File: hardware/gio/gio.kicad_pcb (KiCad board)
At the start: 2 copper layers, 20 x 108 mm, 55 parts, among them J1 PJ3001F, J2 PJ3001F, J3 oled, J4 eurorack power, J5 PJ3001F, J6 PJ3001F, SW1 encoder, U1 TL072, U2 MCP3208, U3 DAC8552, U5 TL072, U6 AMS1117CD-5.0, U7 REF3040, U8 XIAO-RP2350-DIP_pins_only

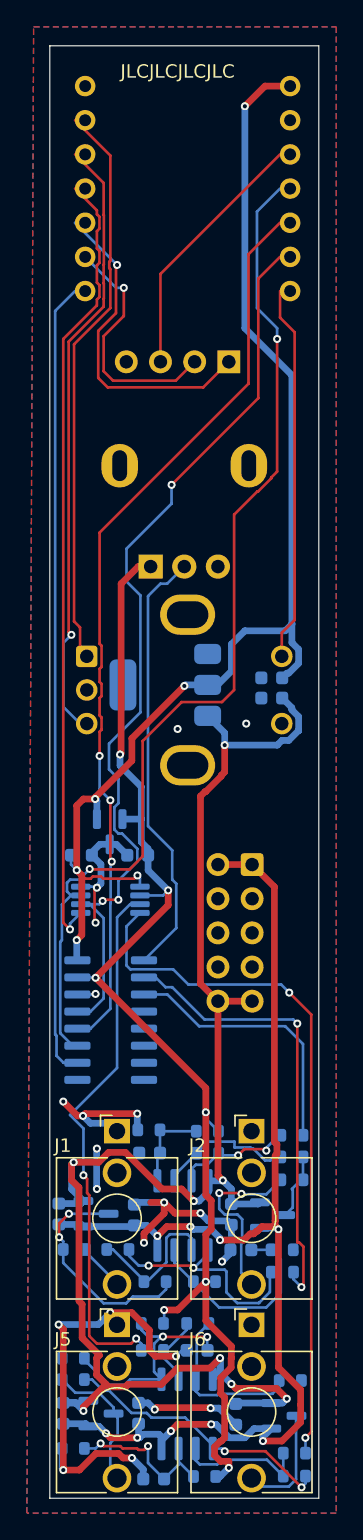
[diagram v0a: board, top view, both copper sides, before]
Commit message: PCB routing progress + zone min_clearance relaxed to 0
Continuation of the layout work from "just ratsnest" (672885e). The
project file also drops board.design_settings.rules.zones.min_clearance
from 0.5 mm to 0.0 — a deliberate design-rule relaxation, not an
autosave artifact.

Co-Authored-By: Claude Opus 4.7 (1M context) <noreply@anthropic.com>
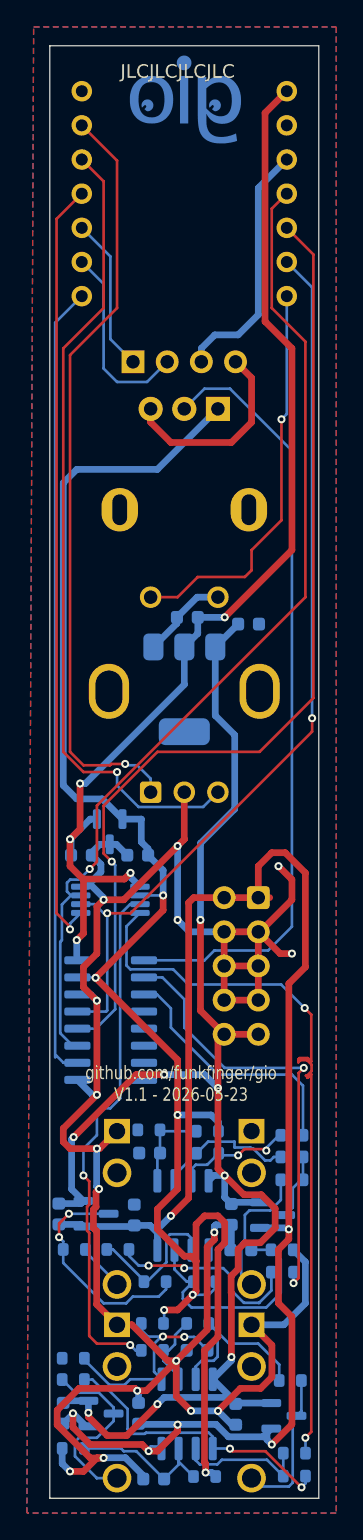
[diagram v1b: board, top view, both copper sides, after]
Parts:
- added G***: LOGO, my_kicad_library:gio-logo, F.Cu at (42.0, 36.0)
- added funkfinger logo 9mm: funkfinger logo 9mm, my_kicad_library:funkfinger-logo-15mm, B.Cu at (41.5, 47.0)
- J3: moved to B.Cu
- moved RV1 12.7 mm to (44.0, 59.0), turned to -90 degrees
- moved SW1 11.2 mm to (39.0, 87.5), turned to 90 degrees
- moved C12 7.72 mm to (41.7, 74.5)
- moved J3 7.12 mm to (37.7, 55.5)
- moved C11 5.76 mm to (46.3, 75.0), turned to 0 degrees
- moved J4 2.50 mm to (47.0, 95.3)
- moved U6 1.45 mm to (41.5, 79.8), turned to -90 degrees
- moved U8 0.46 mm to (41.5, 43.0)
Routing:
- net GND: track 82.3 -> 193.6 mm, vias 21 -> 16
- net /vref: track 91.7 -> 124.5 mm, vias 7 -> 6
- net -12V: track 90.7 -> 119.9 mm, vias 9 -> 6
- net /adc_ch0: track 32.5 -> 58.0 mm
- net /ENCODER_B: track 45.2 -> 60.2 mm
- net /ENCODER_A: track 42.3 -> 57.0 mm, vias 0 -> 1
- net /I2C_SDA: track 24.2 -> 11.5 mm, vias 1 -> 0
- net +5V: track 92.4 -> 83.9 mm, vias 6 -> 5
- net /SPI_MISO: track 67.8 -> 73.7 mm, vias 3 -> 1
- net /out_a: track 9.98 -> 14.1 mm
- net /I2C_SCL: track 18.3 -> 14.4 mm, vias 1 -> 0
- net +12V: track 117.6 -> 114.4 mm
- net /dac_a: track 52.4 -> 55.5 mm
- net /SPI_MOSI: track 78.1 -> 75.2 mm, vias 2 -> 1
- net Net-(J2-PadT): track 12.7 -> 10.2 mm, vias 2 -> 0
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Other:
- board text added: "github.com/funkfinger/gio V1.1 - 2026-05-23"
- board text added: "horray beer"
- board text removed: "red stripe"

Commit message: Hardware Rev 1.1: PCB routing finalized + schematic wire cleanup
Rev 1.1 captures the PCB layout state the user is ready to manufacture
the next batch from. Builds on the Rev 1 bring-up findings (board
electrically validated end-to-end; OLED footprint bug + ADC input
protection captured as Rev 2 to-do items in docs/bench-log.md).

Co-Authored-By: Claude Opus 4.7 (1M context) <noreply@anthropic.com>
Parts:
- removed G***: LOGO, my_kicad_library:gio-logo
- added REF**: OSHW-Logo2_6mm-front-silkscreen, my_kicad_library:OSHW-Logo2_6mm-front-silkscreen, F.Cu at (36.5, 104.0)
- added gio logo: , my_kicad_library:gio-logo-front-copper-mask, B.Cu at (41.5, 36.5)
- funkfinger logo 9mm: footprint my_kicad_library:funkfinger-logo-15mm -> my_kicad_library:funkfinger-logo-9mm-copper-mask
- moved funkfinger logo 9mm 2.00 mm to (41.5, 49.0)
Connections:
- J3 pad 1: /I2C_SDA -> GND
- J3 pad 2: /I2C_SCL -> +3.3V
- J3 pad 3: +3.3V -> /I2C_SCL
- J3 pad 4: GND -> /I2C_SDA
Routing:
- net GND: track 193.6 -> 182.9 mm
- net /I2C_SDA: track 11.5 -> 18.1 mm
- net +3.3V: track 18.7 -> 24.1 mm
